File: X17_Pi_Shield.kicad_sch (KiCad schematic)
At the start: 0 parts

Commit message: Finalized Footprints
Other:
- sheet Pi + IMU ports: added ISO_FLT, NRST_TB; removed none
- sheet UART ports: added ISO_FLT, NRST_TB; removed none

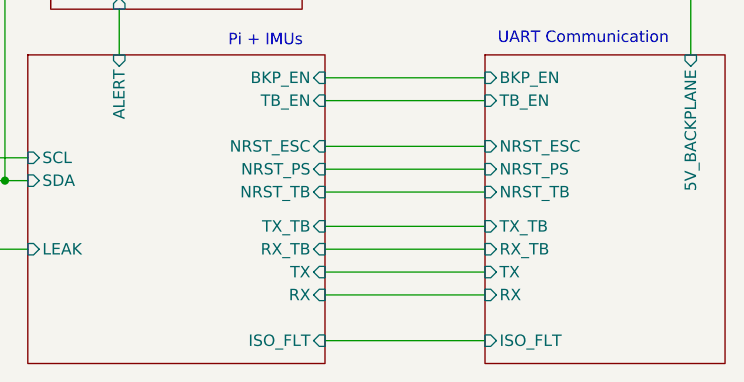
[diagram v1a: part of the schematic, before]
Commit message: fixed several DRC errors and ferrite bead package size, still reviewing the board
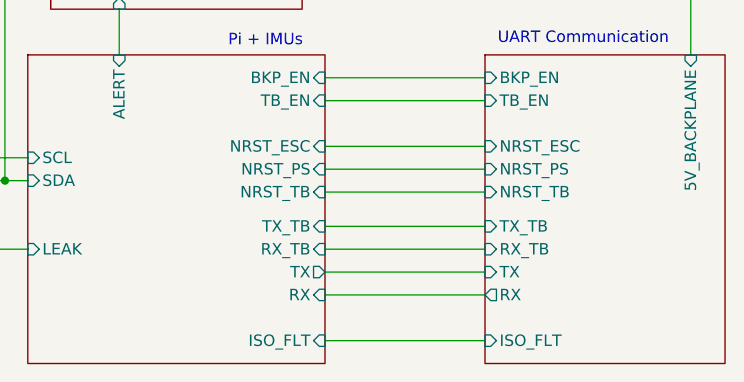
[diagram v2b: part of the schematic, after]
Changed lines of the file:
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@@
 			)
 		)
-		(pin "TX" input
+		(pin "TX" output
 			(at 158.75 116.84 0)
 			(effects
@@
 			)
 		)
-		(pin "RX" input
+		(pin "RX" output
 			(at 176.53 119.38 180)
 			(effects
